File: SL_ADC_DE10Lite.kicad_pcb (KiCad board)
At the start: 4 copper layers, 98 x 67 mm, 33 parts, among them J1 DE10Lite header, J2 Analog header

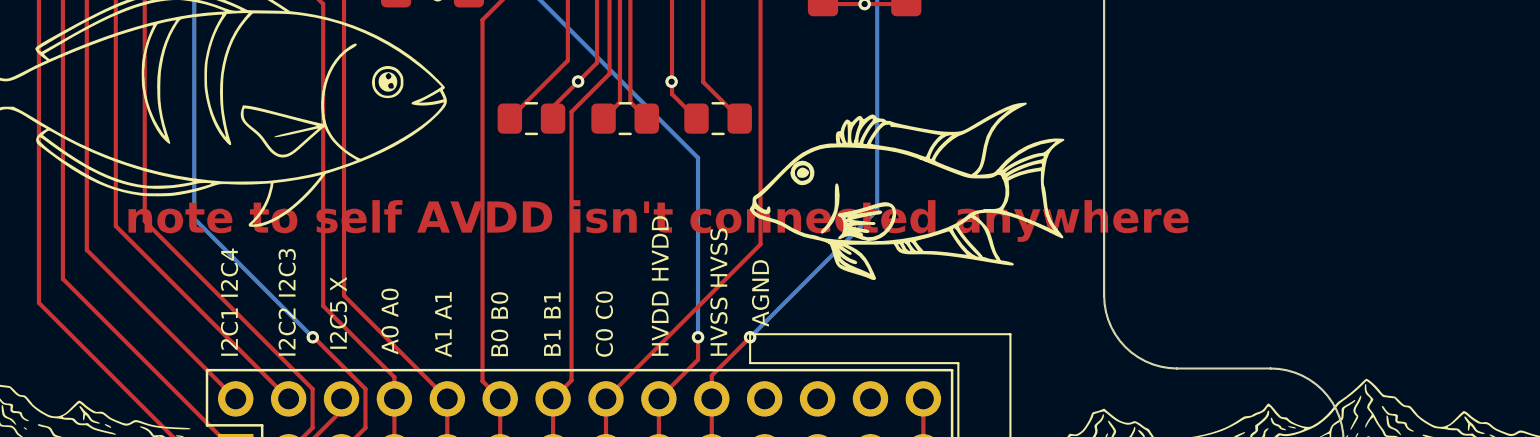
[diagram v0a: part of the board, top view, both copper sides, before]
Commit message: set HVDD to AVDD to share power supply and also updated PCB doc from schematic, re-routing and connecting AVDD to power needed still
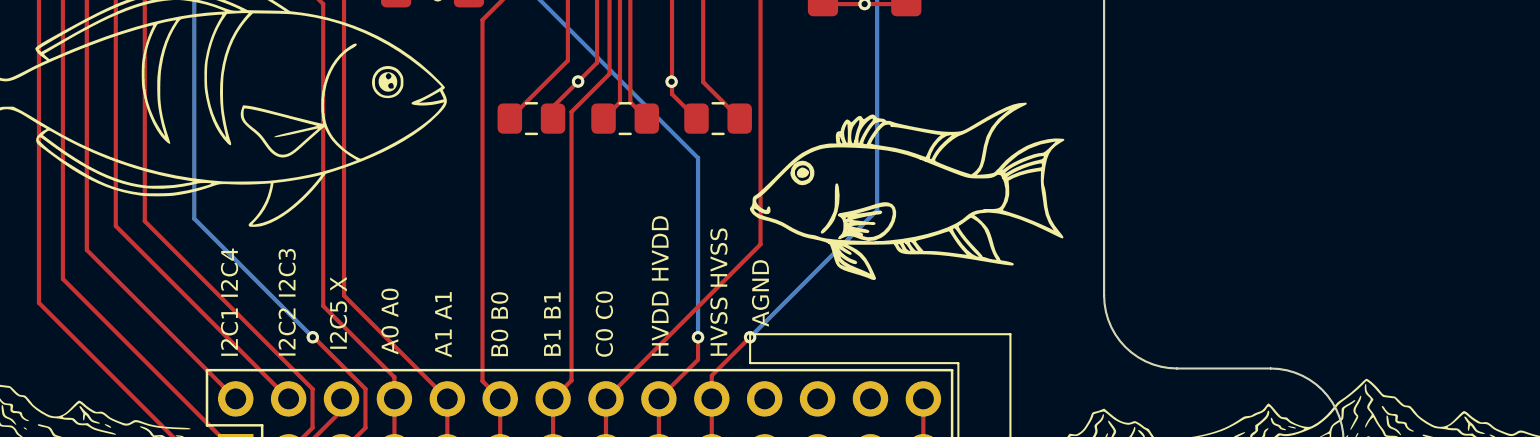
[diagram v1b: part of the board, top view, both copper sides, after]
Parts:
- J2: value Analog header -> Conn_02x14_Odd_Even
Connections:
- C18 pad 1: /HVDD -> /AVDD
- C20 pad 1: /HVDD -> /AVDD
- C5 pad 2: /AGND -> /DGND
- IC1 pad 24: /AGND -> /DGND
- IC1 pad 48: /HVDD -> /AVDD
- J1 pad 12: /AGND -> /DGND
- J1 pad 30: /AGND -> /DGND
- J2 pad 1: /I2C4 -> /DVDD
- J2 pad 10: /CH_A1 -> /I2C5
- J2 pad 11: /CH_B0 -> /AGND
- J2 pad 12: /CH_B0 -> unconnected-(J2-Pin_12-Pad12)
- J2 pad 13: /CH_B1 -> /AGND
- J2 pad 14: /CH_B1 -> /CH_A0
- J2 pad 15: /CH_C0 -> /AGND
- J2 pad 16: /CH_C0 -> /CH_A1
- J2 pad 17: /HVDD -> /AGND
- J2 pad 18: /HVDD -> /CH_B0
- J2 pad 19: /HVSS -> /AGND
- J2 pad 20: /HVSS -> /CH_B1
- J2 pad 21: /AGND -> /HVSS
- J2 pad 22: /AGND -> /CH_C0
- J2 pad 23: /AGND -> /HVSS
- J2 pad 24: /AGND -> /CH_C1
- J2 pad 25: /AGND -> /AVDD
- J2 pad 26: /AGND -> /CH_D0
- J2 pad 27: /AGND -> /AVDD
- J2 pad 28: /AGND -> /CH_D1
- J2 pad 3: /I2C3 -> /DVDD
- J2 pad 5: /DVDD -> /AGND
- J2 pad 6: /I2C5 -> /I2C3
- J2 pad 7: /CH_A0 -> /AGND
- J2 pad 8: /CH_A0 -> /I2C4
- J2 pad 9: /CH_A1 -> /AGND
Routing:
- net /HVDD: track 38.3 -> 0.00 mm, vias 2 -> 0
- net (no net): track 0.00 -> 38.3 mm
- net /AGND: track 112.6 -> 108.3 mm
- net /DGND: track 0.00 -> 4.35 mm
- net /CH_B0: vias 0 -> 2
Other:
- board text removed: "note to self AVDD isn't connected anywhere"

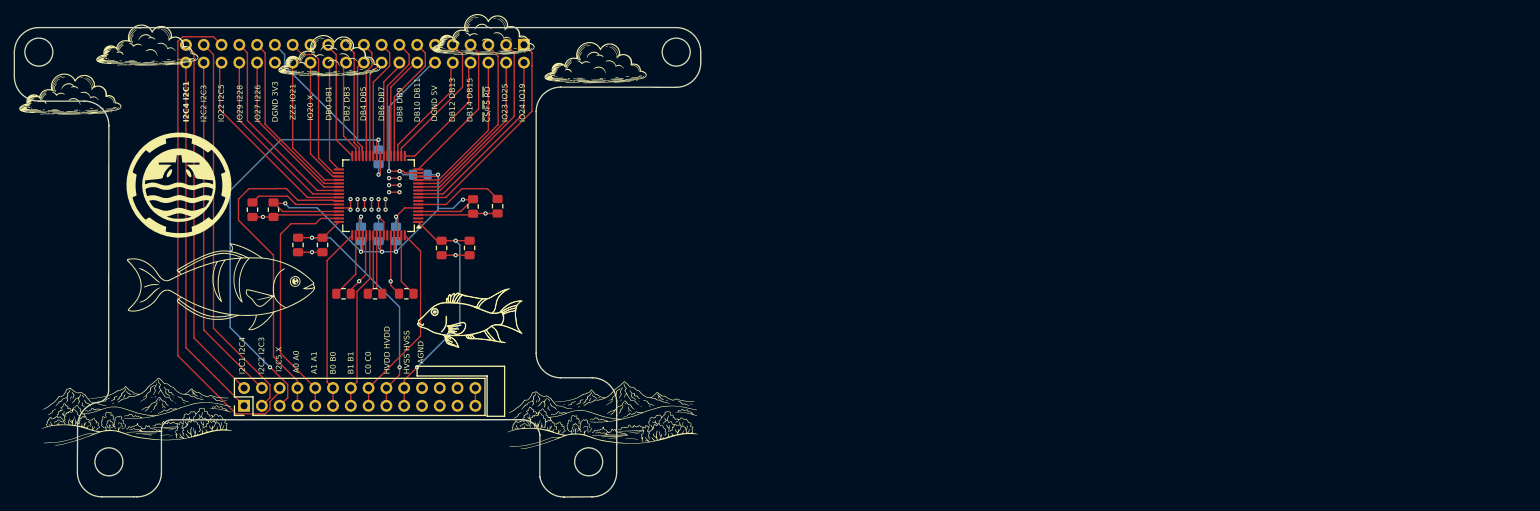
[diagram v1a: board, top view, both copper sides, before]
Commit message: updated PCB to match foodtprint header pinout, flagged issues with ground planes only being on one layer and not being under all the relevant pins. Re-routing and ground plane re-shaping needed
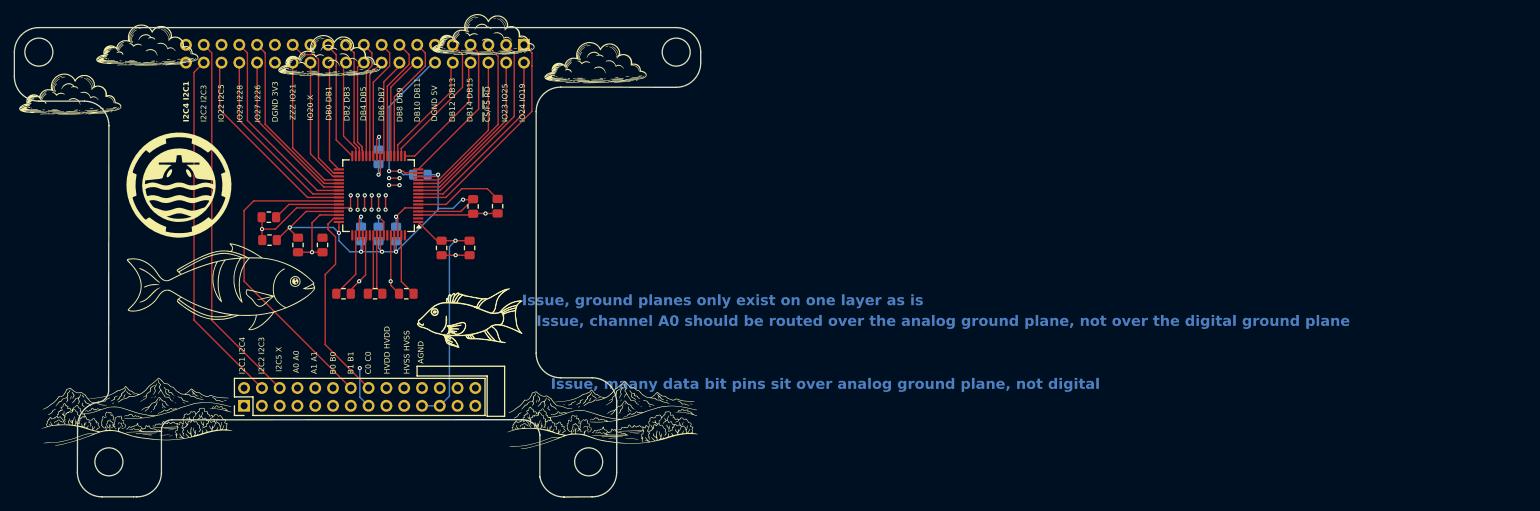
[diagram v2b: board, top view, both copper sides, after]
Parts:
- moved C3 4.38 mm to (96.4, 80.3), turned to 180 degrees
- moved C8 2.57 mm to (96.3, 77.1), turned to 180 degrees
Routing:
- net /DVDD: track 84.1 -> 4.73 mm, vias 2 -> 1
- net (no net): track 38.3 -> 0.00 mm
- net /CH_C0: track 28.3 -> 0.00 mm
- net /CH_B0: track 26.2 -> 0.00 mm, vias 2 -> 0
- net /CH_B1: track 25.5 -> 0.00 mm
- net /AGND: track 108.3 -> 125.1 mm, vias 30 -> 29
- net /I2C5: track 72.3 -> 55.5 mm
- net /CH_A1: track 35.8 -> 28.9 mm
- net /REFAP: track 13.2 -> 9.73 mm
- net /CH_A0: track 48.4 -> 45.8 mm
- net /I2C3: track 55.9 -> 53.5 mm
- net /I2C2: track 49.9 -> 51.0 mm
- net /AVDD: track 74.4 -> 75.4 mm, vias 6 -> 7
- net /I2C1: track 52.4 -> 53.4 mm
- net /I2C4: track 52.4 -> 53.1 mm
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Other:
- board text added: "Issue, channel A0 should be routed over the analog ground plane, not over the digital ground plane"
- board text added: "Issue, ground planes only exist on one layer as is"
- board text added: "Issue, maany data bit pins sit over analog ground plane, not digital"

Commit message: Re routed, reshaped ground planes and included on both layers, next, add silkscreens
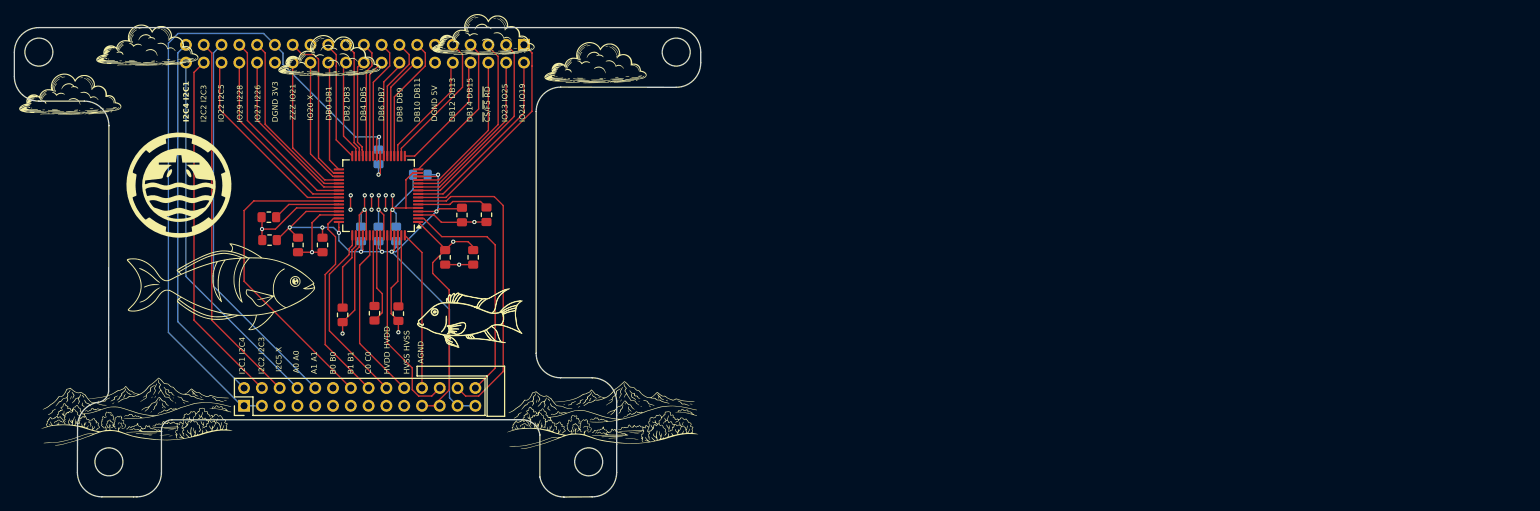
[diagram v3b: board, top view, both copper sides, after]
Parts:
- moved C23 3.06 mm to (114.8, 90.8), turned to -90 degrees
- moved C9 3.02 mm to (106.9, 91.0), turned to -90 degrees
- moved C16 2.78 mm to (111.4, 90.8), turned to 90 degrees
- moved C1 2.01 mm to (123.9, 76.8)
- moved C24 2.01 mm to (127.4, 76.7)
- moved C19 1.44 mm to (121.5, 82.8)
- moved C21 1.44 mm to (125.5, 82.8)
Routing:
- net /DVDD: track 4.73 -> 101.4 mm
- net /CH_D0: track 0.00 -> 45.4 mm
- net /CH_D1: track 0.00 -> 34.2 mm
- net /CH_C1: track 0.00 -> 28.3 mm
- net /CH_B0: track 0.00 -> 27.4 mm
- net /CH_B1: track 0.00 -> 25.0 mm
- net /CH_C0: track 0.00 -> 22.8 mm
- net /AVDD: track 75.4 -> 98.0 mm, vias 7 -> 8
- net /AGND: track 125.1 -> 117.2 mm, vias 29 -> 11
- net /DGND: track 4.35 -> 10.5 mm, vias 0 -> 8
- net /REFIO: track 8.66 -> 12.9 mm
- net /HVSS: track 35.5 -> 38.4 mm
- net /REFDP: track 12.9 -> 10.3 mm
- net /REFN: track 8.66 -> 10.2 mm
- net /REFCP: track 9.06 -> 10.3 mm
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- added copper zone on In1.Cu, net /DGND
- added copper zone on In2.Cu, net /DGND
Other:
- board text added: "IC1"
- board text removed: "Issue, channel A0 should be routed over the analog ground plane, not over the digital ground plane"
- board text removed: "Issue, ground planes only exist on one layer as is"
- board text removed: "Issue, maany data bit pins sit over analog ground plane, not digital"

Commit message: fixed some DRC issues
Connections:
- C5 pad 2: /DGND -> /AGND
- IC1 pad 24: /DGND -> /AGND
- J1 pad 12: /DGND -> /AGND
- J1 pad 30: /DGND -> /AGND
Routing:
- net /AGND: track 117.2 -> 127.7 mm, vias 11 -> 19
- net /DGND: track 10.5 -> 0.00 mm, vias 8 -> 0
- removed copper zone on In1.Cu, net /DGND
- removed copper zone on In2.Cu, net /DGND
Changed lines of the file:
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@@
 			(layers "F.Cu" "F.Mask" "F.Paste")
 			(roundrect_rratio 0.25)
-			(net "/DGND")
+			(net "/AGND")
 			(pinfunction "DGND_24")
 			(pintype "power_in")
@@
 			(layers "*.Cu" "*.Mask")
 			(remove_unused_layers no)
-			(net "/DGND")
+			(net "/AGND")
 			(pinfunction "Pin_12_12")
 			(pintype "passive")
@@
 			(layers "*.Cu" "*.Mask")
 			(remove_unused_layers no)
-			(net "/DGND")
+			(net "/AGND")
 			(pinfunction "Pin_30_30")
 			(pintype "passive")
@@
 			(layers "B.Cu" "B.Mask" "B.Paste")
 			(roundrect_rratio 0.212766)
-			(net "/DGND")
+			(net "/AGND")
 			(pintype "passive")
 		)
@@
 		)
 	)
-	(gr_poly
-		(pts
-			(xy 127.5 105.5) (xy 130 105.5) (xy 130 98.353332) (xy 117.5 98.353332) (xy 117.5 99.741362) (xy 127.5 99.741362)
-		)
-		(stroke
-			(width 0.1)
-			(type solid)
-		)
-		(fill cross_hatch)
-		(layer "F.SilkS")
-	)
 	(gr_arc
 		(start 60 53.5)
@@
 	)
 	(gr_text "AGND"
-		(at 118.5 98 90)
+		(at 118.61 99.44 90)
+		(layer "F.SilkS")
+		(effects
+			(font
+				(size 0.8 0.8)
+				(thickness 0.1)
+			)
+			(justify left bottom)
+		)
+	)
+	(gr_text "AGND"
+		(at 121.09 99.72 90)
 		(layer "F.SilkS")
 		(effects
@@
 		)
 	)
+	(gr_text "AGND"
+		(at 123.8 100.03 90)
+		(layer "F.SilkS")
+		(effects
+			(font
+				(size 0.8 0.8)
+				(thickness 0.1)
+			)
+			(justify left bottom)
+		)
+	)
 	(gr_text "DB14 DB15\n"
 		(at 125.5 63.5 90)
@@
 		)
 	)
+	(gr_text "AGND"
+		(at 126.43 99.84 90)
+		(layer "F.SilkS")
+		(effects
+			(font
+				(size 0.8 0.8)
+				(thickness 0.1)
+			)
+			(justify left bottom)
+		)
+	)
 	(gr_text "~{CS}/~{F5} ~{RD}\n"
 		(at 128 63.5 90)
@@
 	)
 	(segment
+		(start 112 71)
+		(end 112.25 70.75)
+		(width 0.2)
+		(layer "F.Cu")
+		(net "/AGND")
+	)
+	(segment
 		(start 102.5 82.075)
 		(end 100.5 82.075)
@@
 	)
 	(segment
+		(start 108 76)
+		(end 108 73.98)
+		(width 0.2)
+		(layer "F.Cu")
+		(net "/AGND")
+	)
+	(segment
 		(start 109.25 79.6625)
 		(end 109.25 81.31)
@@
 	)
 	(segment
+		(start 112.25 70.75)
+		(end 112.25 68.3375)
+		(width 0.2)
+		(layer "F.Cu")
+		(net "/AGND")
+	)
+	(segment
 		(start 108.6 90.3275)
 		(end 106.87 92.0575)
@@
 	)
 	(segment
+		(start 111 76)
+		(end 111 73.98)
+		(width 0.2)
+		(layer "F.Cu")
+		(net "/AGND")
+	)
+	(segment
 		(start 103.61 76.75)
 		(end 102.5 77.86)
@@
 	)
 	(segment
+		(start 113 73.98)
+		(end 113.03 73.95)
+		(width 0.2)
+		(layer "F.Cu")
+		(net "/AGND")
+	)
+	(segment
 		(start 117.6625 75.75)
 		(end 115.91 75.75)
@@
 	)
 	(segment
+		(start 113 76)
+		(end 113 73.98)
+		(width 0.2)
+		(layer "F.Cu")
+		(net "/AGND")
+	)
+	(segment
+		(start 108 73.98)
+		(end 108.03 73.95)
+		(width 0.2)
+		(layer "F.Cu")
+		(net "/AGND")
+	)
+	(segment
 		(start 119.921471 76.75)
 		(end 120.968971 77.7975)
@@
 	)
 	(segment
+		(start 111 73.98)
+		(end 111.03 73.95)
+		(width 0.2)
+		(layer "F.Cu")
+		(net "/AGND")
+	)
+	(segment
 		(start 115.91 71.73259)
 		(end 115.91 75.75)
@@
 	)
 	(via
+		(at 110.03 73.95)
+		(size 0.6)
+		(drill 0.3)
+		(layers "F.Cu" "B.Cu")
+		(free yes)
+		(net "/AGND")
+	)
+	(via
+		(at 113.03 73.95)
+		(size 0.6)
+		(drill 0.3)
+		(layers "F.Cu" "B.Cu")
+		(free yes)
+		(net "/AGND")
+	)
+	(via
 		(at 123.51125 83.845)
 		(size 0.6)
@@
 	)
 	(via
+		(at 112.03 73.95)
+		(size 0.6)
+		(drill 0.3)
+		(layers "F.Cu" "B.Cu")
+		(free yes)
+		(net "/AGND")
+	)
+	(via
+		(at 114.02 73.96)
+		(size 0.6)
+		(drill 0.3)
+		(layers "F.Cu" "B.Cu")
+		(free yes)
+		(net "/AGND")
+	)
+	(via
+		(at 111.03 73.95)
+		(size 0.6)
+		(drill 0.3)
+		(layers "F.Cu" "B.Cu")
+		(free yes)
+		(net "/AGND")
+	)
+	(via
 		(at 106.86 93.69)
 		(size 0.6)
@@
 	)
 	(via
+		(at 112 71)
+		(size 0.6)
+		(drill 0.3)
+		(layers "F.Cu" "B.Cu")
+		(free yes)
+		(net "/AGND")
+	)
+	(via
+		(at 108 76)
+		(size 0.6)
+		(drill 0.3)
+		(layers "F.Cu" "B.Cu")
+		(net "/AGND")
+	)
+	(via
+		(at 108.03 73.95)
+		(size 0.6)
+		(drill 0.3)
+		(layers "F.Cu" "B.Cu")
+		(free yes)
+		(net "/AGND")
+	)
+	(via
 		(at 114.83 93.5)
 		(size 0.6)
@@
 	)
 	(segment
+		(start 96.94 55)
+		(end 97 55.06)
+		(width 0.2)
+		(layer "B.Cu")
+		(net "/AGND")
+	)
+	(segment
 		(start 114.5 76.52)
 		(end 113.99 76.01)
@@
 	)
 	(segment
+		(start 112 69.5)
+		(end 112 71)
+		(width 0.2)
+		(layer "B.Cu")
+		(net "/AGND")
+	)
+	(segment
 		(start 109.5 76.5)
 		(end 110 76)
@@
 	)
 	(segment
-		(start 112 71)
-		(end 112.25 70.75)
-		(width 0.2)
-		(layer "F.Cu")
-		(net "/DGND")
-	)
-	(segment
-		(start 108 76)
-		(end 108 73.98)
-		(width 0.2)
-		(layer "F.Cu")
-		(net "/DGND")
-	)
-	(segment
-		(start 112.25 70.75)
-		(end 112.25 68.3375)
-		(width 0.2)
-		(layer "F.Cu")
-		(net "/DGND")
-	)
-	(segment
-		(start 111 76)
-		(end 111 73.98)
-		(width 0.2)
-		(layer "F.Cu")
-		(net "/DGND")
-	)
-	(segment
-		(start 113 73.98)
-		(end 113.03 73.95)
-		(width 0.2)
-		(layer "F.Cu")
-		(net "/DGND")
-	)
-	(segment
-		(start 113 76)
-		(end 113 73.98)
-		(width 0.2)
-		(layer "F.Cu")
-		(net "/DGND")
-	)
-	(segment
-		(start 108 73.98)
-		(end 108.03 73.95)
-		(width 0.2)
-		(layer "F.Cu")
-		(net "/DGND")
-	)
-	(segment
-		(start 111 73.98)
-		(end 111.03 73.95)
-		(width 0.2)
-		(layer "F.Cu")
-		(net "/DGND")
-	)
-	(via
-		(at 110.03 73.95)
-		(size 0.6)
-		(drill 0.3)
-		(layers "F.Cu" "B.Cu")
-		(free yes)
-		(net "/DGND")
-	)
-	(via
-		(at 113.03 73.95)
-		(size 0.6)
-		(drill 0.3)
-		(layers "F.Cu" "B.Cu")
-		(free yes)
-		(net "/DGND")
-	)
-	(via
-		(at 112.03 73.95)
-		(size 0.6)
-		(drill 0.3)
-		(layers "F.Cu" "B.Cu")
-		(free yes)
-		(net "/DGND")
-	)
-	(via
-		(at 114.02 73.96)
-		(size 0.6)
-		(drill 0.3)
-		(layers "F.Cu" "B.Cu")
-		(free yes)
-		(net "/DGND")
-	)
-	(via
-		(at 111.03 73.95)
-		(size 0.6)
-		(drill 0.3)
-		(layers "F.Cu" "B.Cu")
-		(free yes)
-		(net "/DGND")
-	)
-	(via
-		(at 112 71)
-		(size 0.6)
-		(drill 0.3)
-		(layers "F.Cu" "B.Cu")
-		(free yes)
-		(net "/DGND")
-	)
-	(via
-		(at 108 76)
-		(size 0.6)
-		(drill 0.3)
-		(layers "F.Cu" "B.Cu")
-		(net "/DGND")
-	)
-	(via
-		(at 108.03 73.95)
-		(size 0.6)
-		(drill 0.3)
-		(layers "F.Cu" "B.Cu")
-		(free yes)
-		(net "/DGND")
-	)
-	(segment
-		(start 96.94 55)
-		(end 97 55.06)
-		(width 0.2)
-		(layer "B.Cu")
-		(net "/DGND")
-	)
-	(segment
-		(start 112 69.5)
-		(end 112 71)
-		(width 0.2)
-		(layer "B.Cu")
-		(net "/DGND")
-	)
-	(segment
 		(start 111.75 68.3375)
 		(end 111.75 65.93)
@@
 	)
 	(zone
-		(net "/DGND")
+		(net "/AGND")
 		(layers "In1.Cu" "In2.Cu")
 		(hatch edge 0.5)
